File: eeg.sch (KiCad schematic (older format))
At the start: 145 parts, among them J1 USB_B_Mini, U1 STM32F446RE, U10 -.+2.5V.+3.3V-GND, U11 +5V, U12 RN4678-V_RM100, U13 ADS1299IPAG, U2 ADS1299-8CHANNEL, U3 LD39050PU33R, U4 TPS60403DBVT, U5 TPS73225DBVT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

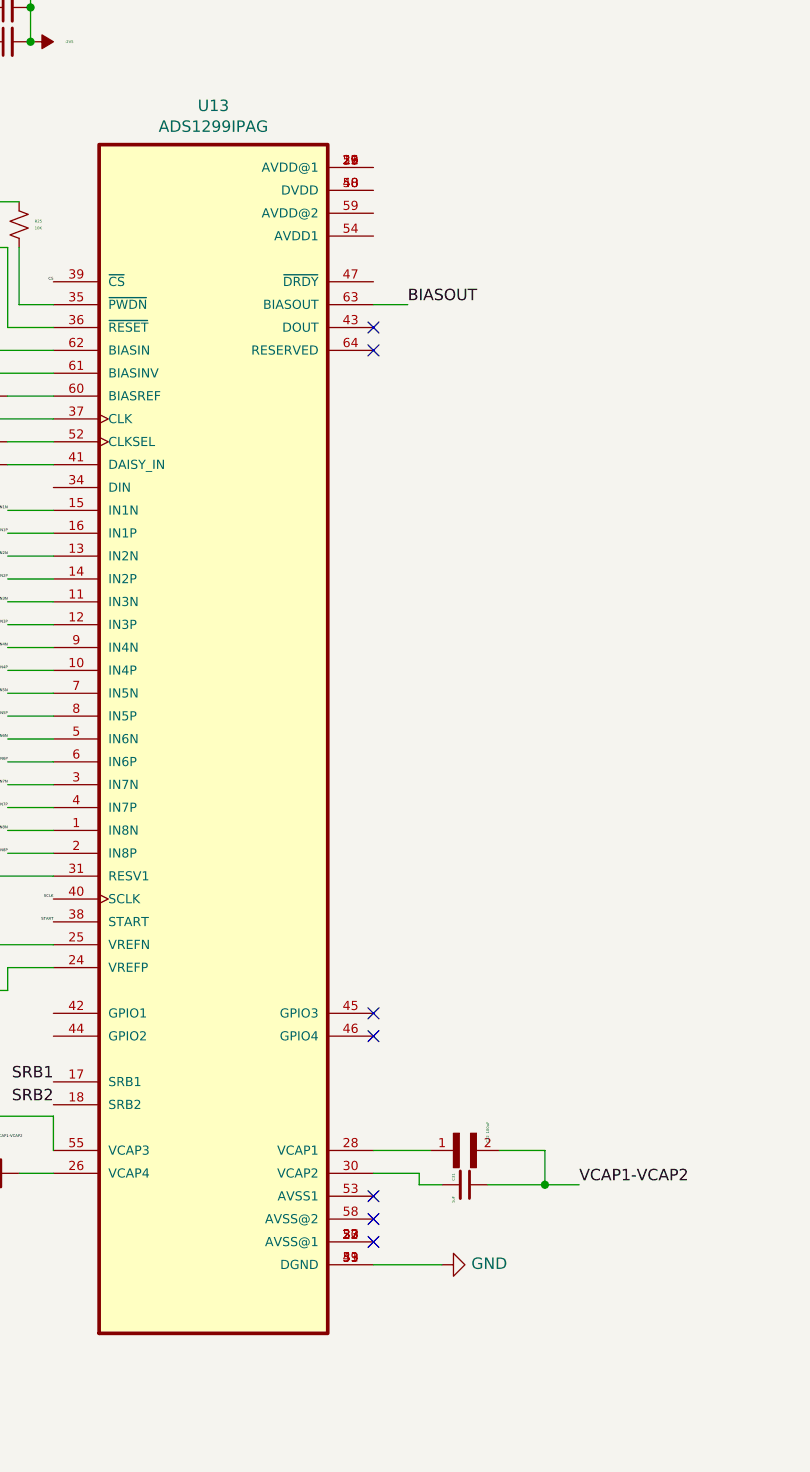
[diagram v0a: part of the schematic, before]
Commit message: ADS1299's SPI connections fixed and Supply pins should be checked
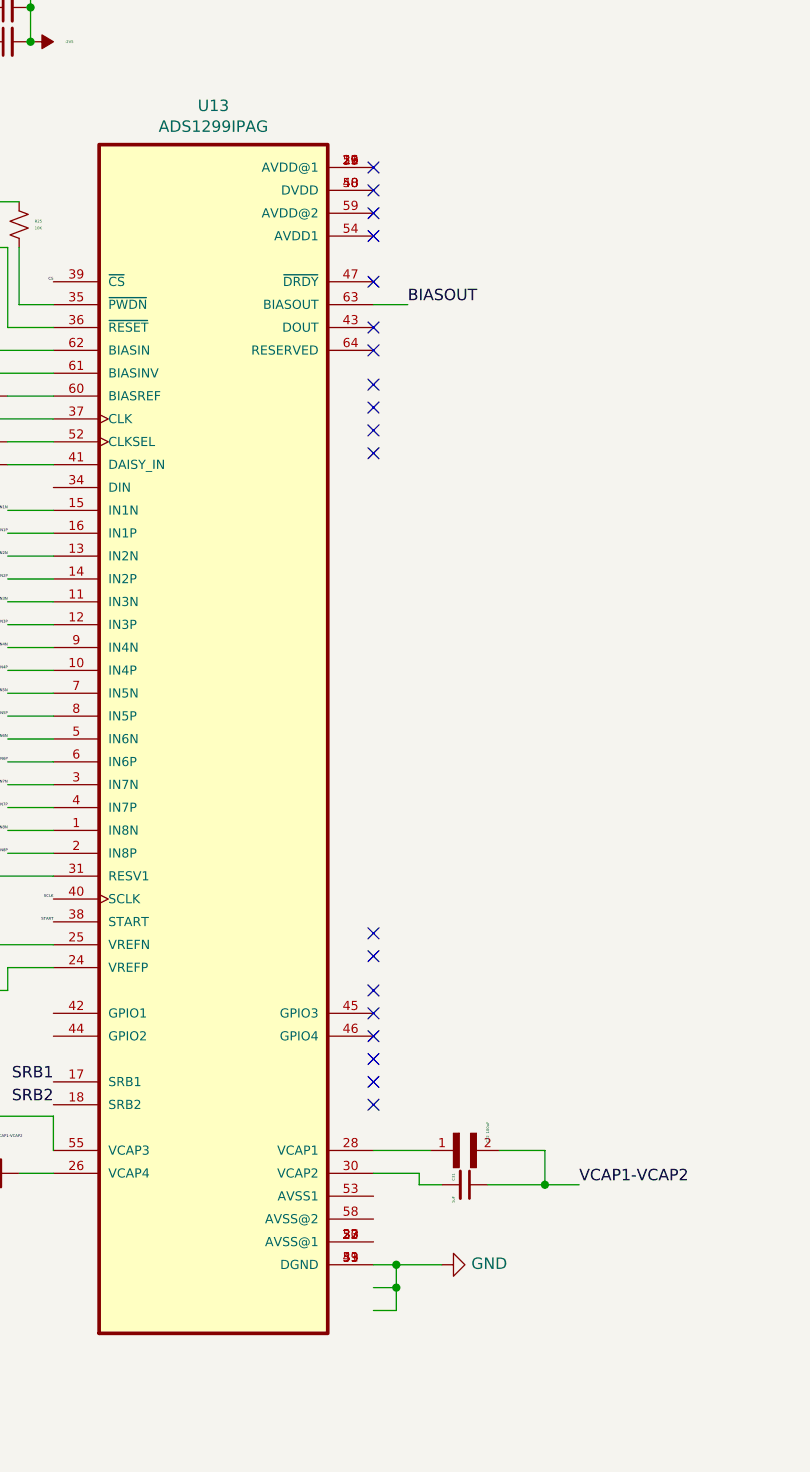
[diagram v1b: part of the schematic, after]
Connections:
- no-connect marks 82 -> 94
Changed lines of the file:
@@
-	1    0    0    -1
-$EndComp
-$Comp
-L ADS1299IPAG:ADS1299IPAG U13
-U 1 1 6000F5DE
-P 7350 13100
-F 0 "U13" H 7350 15870 50  0000 C CNN
-F 1 "ADS1299IPAG" H 7350 15779 50  0000 C CNN
-F 2 "QFP50P1200X1200X120-64N" H 7350 13100 50  0001 L BNN
-F 3 "" H 7350 13100 50  0001 L BNN
-	1    7350 13100
 	1    0    0    -1
 $EndComp
@@
 $EndComp
 Wire Wire Line
-	8050 15400 8350 15400
+	8050 15400 8150 15400
 Wire Wire Line
 	6300 15000 5950 15000
@@
 NoConn ~ 8050 14300
 NoConn ~ 8050 14400
-NoConn ~ 8050 15100
-NoConn ~ 8050 15200
-NoConn ~ 8050 15300
 NoConn ~ 8050 11300
 NoConn ~ 8050 11400
@@
 Wire Wire Line
 	12700 6650 12700 7150
+$Comp
+L ADS1299IPAG:ADS1299IPAG U13
+U 1 1 6000F5DE
+P 7350 13100
+F 0 "U13" H 7350 15870 50  0000 C CNN
+F 1 "ADS1299IPAG" H 7350 15779 50  0000 C CNN
+F 2 "QFP50P1200X1200X120-64N" H 7350 13100 50  0001 L BNN
+F 3 "" H 7350 13100 50  0001 L BNN
+	1    7350 13100
+	1    0    0    -1
+$EndComp
+Wire Wire Line
+	8050 15500 8150 15500
+Wire Wire Line
+	8150 15500 8150 15400
+Connection ~ 8150 15400
+Wire Wire Line
+	8150 15400 8350 15400
+Wire Wire Line
+	8050 15600 8150 15600
+Wire Wire Line
+	8150 15600 8150 15500
+Connection ~ 8150 15500
+NoConn ~ 8050 13950
+NoConn ~ 8050 14050
+NoConn ~ 8050 14200
+NoConn ~ 8050 14500
+NoConn ~ 8050 14600
+NoConn ~ 8050 14700
+NoConn ~ 8050 11550
+NoConn ~ 8050 11650
+NoConn ~ 8050 11750
+NoConn ~ 8050 11850
+NoConn ~ 8050 11100
+NoConn ~ 8050 10600
+NoConn ~ 8050 10700
+NoConn ~ 8050 10800
+NoConn ~ 8050 10900
 $EndSCHEMATC

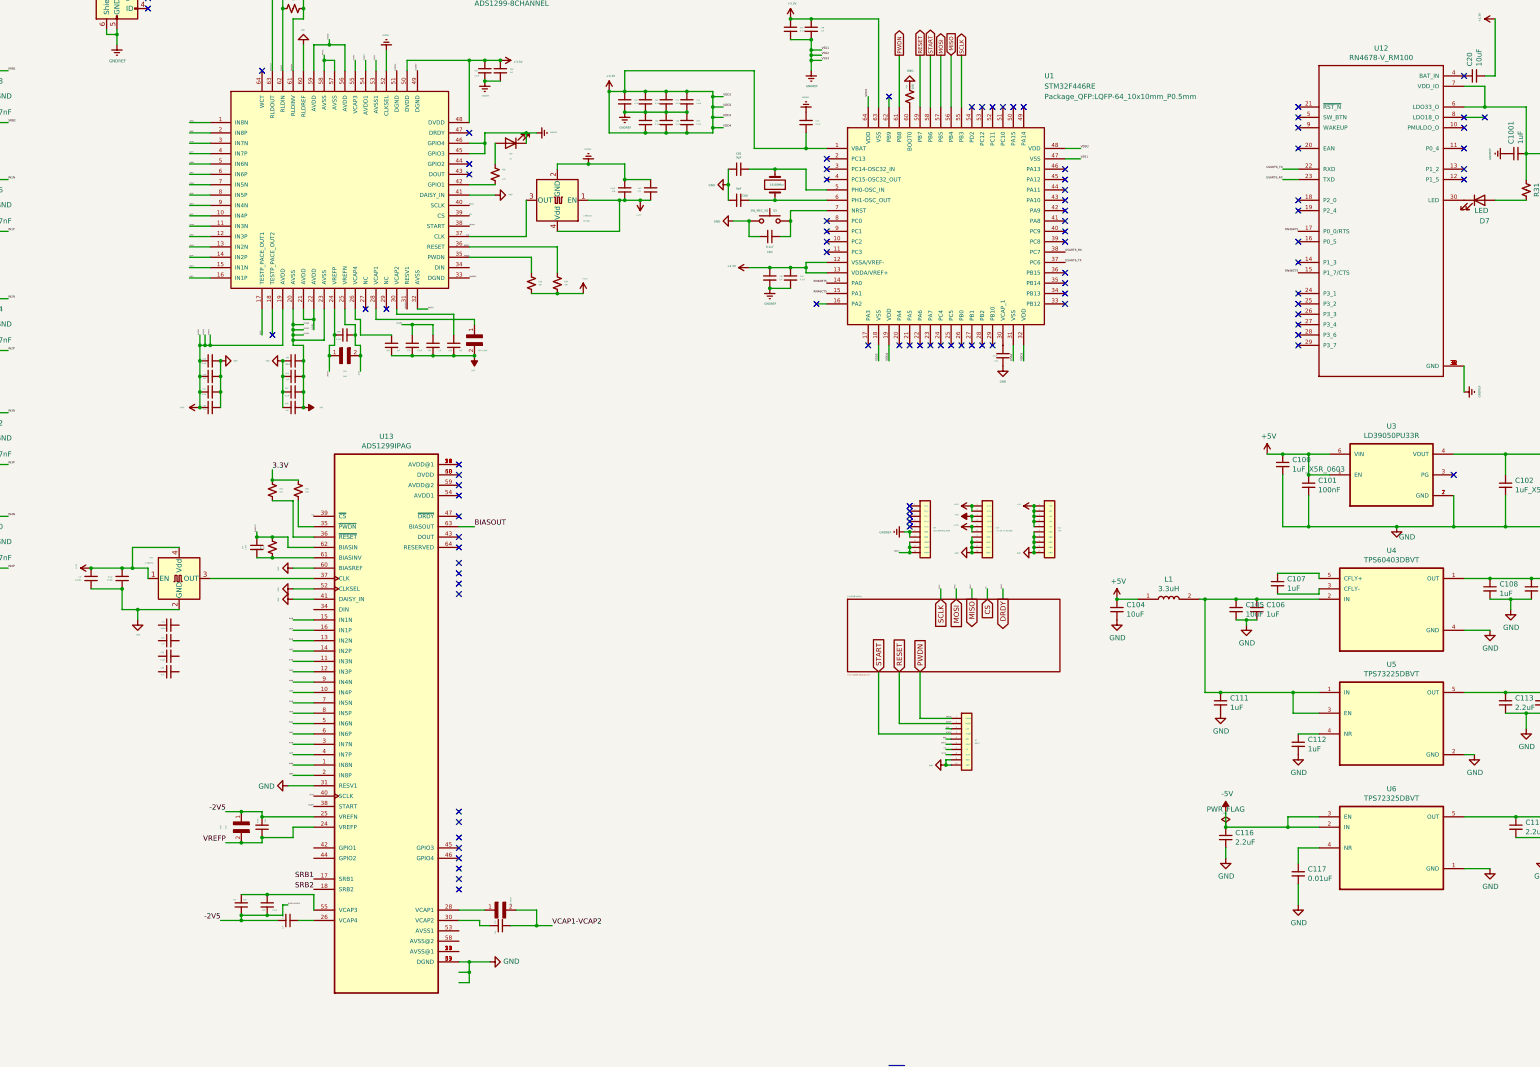
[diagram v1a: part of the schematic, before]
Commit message: ADS1299 Tracks fixed.
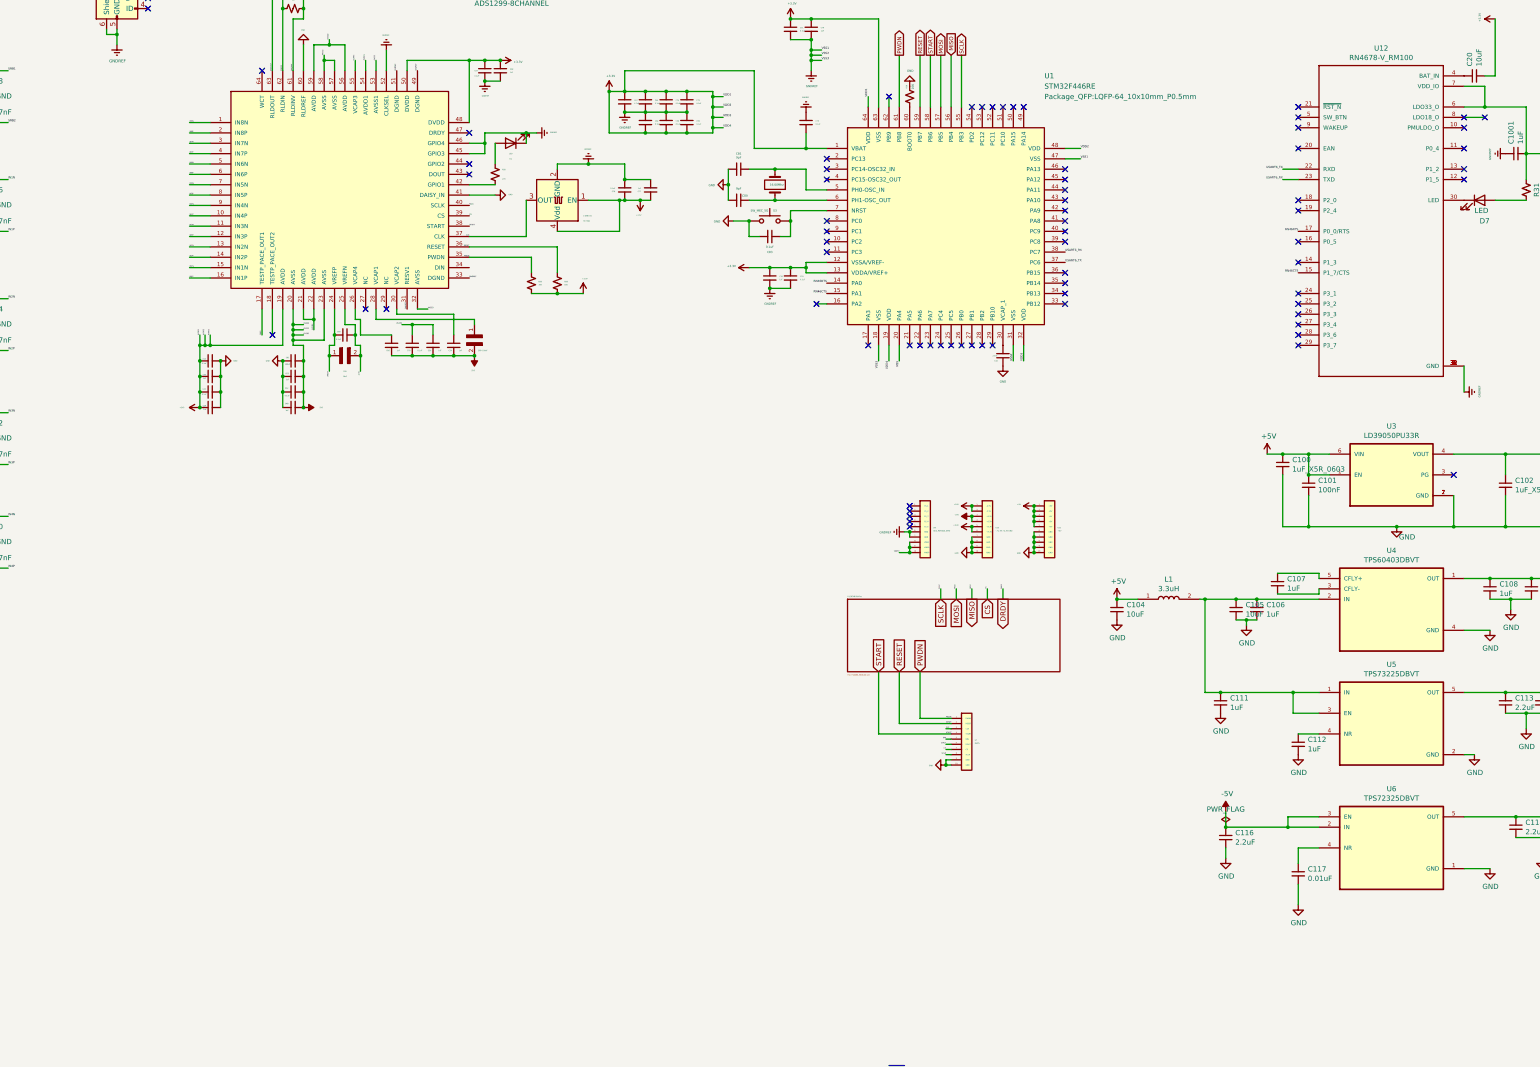
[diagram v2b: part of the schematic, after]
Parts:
- removed C1000, C23, C28, C29: 0.1uF, Capacitor_SMD:C_0603_1608Metric, symbol Device:C_Small
- removed C10001, C22, C24, C26, C30, C31: 1uF, Capacitor_SMD:C_0603_1608Metric, symbol Device:C_Small
- removed C21: 100uF, Capacitor_SMD:C_0603_1608Metric, symbol Device:C_Small
- removed C25: 10uF, TCA1C106M8R:RESC3216X65N, symbol TCA1C106M8R:TCA1C106M8R
- removed C27: 1.5nF, Capacitor_SMD:C_0805_2012Metric, symbol Device:C_Small
- removed C32: 100uF, TCA1C106M8R:RESC3216X65N, symbol TCA1C106M8R:TCA1C106M8R
- removed HC2: 2.048mhz, ERA-3A:OSCCC500X320X150N, symbol Oscillator:ASE-xxxMHz
- removed R23, R25: 10K, ERA-3A:RESC1608X55N, symbol Device:R_Small_US
- removed R24: 1M, ERA-6AEB105V:RESC2012X60N, symbol Device:R_Small_US
- removed U13: ADS1299IPAG, QFP50P1200X1200X120-64N, symbol ADS1299IPAG:ADS1299IPAG
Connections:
- net NSS: now reaches U1.20 (PA4)
- no-connect marks 94 -> 73

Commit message: Created hierarchical sheet
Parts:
- C65, C69: symbol TCA1C106M8R:TCA1C106M8R -> eeg-rescue:TCA1C106M8R-TCA1C106M8R
- L1, L2, L4, L5: symbol MLZ2012A3R3WT000:MLZ2012A3R3WT000 -> eeg-rescue:MLZ2012A3R3WT000-MLZ2012A3R3WT000
- U3: symbol LD39050PU33R:LD39050PU33R -> eeg-rescue:LD39050PU33R-LD39050PU33R
- U4: symbol TPS60403DBVT:TPS60403DBVT -> eeg-rescue:TPS60403DBVT-TPS60403DBVT
- U5: symbol TPS73225DBVT:TPS73225DBVT -> eeg-rescue:TPS73225DBVT-TPS73225DBVT
- U6: symbol TPS72325DBVT:TPS72325DBVT -> eeg-rescue:TPS72325DBVT-TPS72325DBVT
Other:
- moved on the sheet: C1, C10, C100, C1001, C101, C102, C103, C104, C105, C106, C107, C108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

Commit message: GND changed to GNDA
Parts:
- added D2, D3, D4: LED, LED_SMD:LED_0603_1608Metric, symbol Device:LED
- added J2: Conn_01x10_MountingPin, Connector_PinHeader_1.27mm:PinHeader_1x10_P1.27mm_Vertical, symbol Connector_Generic_MountingPin:Conn_01x10_MountingPin
- added R20, R21, R22: R_Small, symbol Device:R_Small
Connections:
- net labels added: GNDA, GNDD, SWCLK, SWDIO
- wire segments 429 -> 442
- no-connect marks 73 -> 71

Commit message: uC status leds added
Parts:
- removed U61: Electrode1, ADS1299IPAG:openldhardware, symbol eeg-rescue:Electrode-Electrode-eeg-rescue-eeg-rescue
- removed U8: Electrode2, ADS1299IPAG:openldhardware, symbol eeg-rescue:Electrode2-Electrode2
- added J3, J4: Conn_02x20_Counter_Clockwise, Connector_PinHeader_1.27mm:PinHeader_2x20_P1.27mm_Vertical, symbol Connector_Generic:Conn_02x20_Counter_Clockwise
- C1001: footprint (none) -> Capacitor_SMD:C_0603_1608Metric
- D1: footprint (none) -> LED_SMD:LED_0603_1608Metric
- R20, R21, R22: footprint (none) -> Resistor_SMD:R_0603_1608Metric
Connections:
- no-connect marks 71 -> 68

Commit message: SPI3 changed to SPI1
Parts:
- removed J2: Conn_01x10_MountingPin, Connector_PinHeader_1.27mm:PinHeader_1x10_P1.27mm_Vertical, symbol Connector_Generic_MountingPin:Conn_01x10_MountingPin
- removed S3: SW_MEC_5G, Button_Switch_SMD:SW_SPST_B3U-1000P, symbol Switch:SW_MEC_5G
- added J2: Conn_01x10, Connector_PinHeader_1.27mm:PinHeader_1x10_P1.27mm_Vertical, symbol Connector_Generic:Conn_01x10
- added SW3: EVQ-Q2K03W, EVQ-Q2K03W_PAN, symbol 2021-02-28_21-16-32:EVQ-Q2K03W
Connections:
- net labels added: SCK
- net labels removed: GND, NSS
- wire segments 442 -> 445
- no-connect marks 68 -> 65
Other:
- moved on the sheet: C74, C76, C83, D2, D3, D4

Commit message: Connectors change 1.27mm to 2.54mm and 20 pins to 10 pins
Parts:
- removed C1001: 1uF, Capacitor_SMD:C_0603_1608Metric, symbol Device:C_Small
- removed J2: Conn_01x10, Connector_PinHeader_1.27mm:PinHeader_1x10_P1.27mm_Vertical, symbol Connector_Generic:Conn_01x10
- removed J3, J4: Conn_02x20_Counter_Clockwise, Connector_PinHeader_1.27mm:PinHeader_2x20_P1.27mm_Vertical, symbol Connector_Generic:Conn_02x20_Counter_Clockwise
- removed U10: -.+2.5V.+3.3V-GND, Connector_PinSocket_1.27mm:PinSocket_1x10_P1.27mm_Vertical, symbol eeg-rescue:-.+2.5V.+3.3V-GND-Data10Pin
- removed U11: +5V, Connector_PinSocket_1.27mm:PinSocket_1x10_P1.27mm_Vertical, symbol eeg-rescue:+5V-Data10Pin
- removed U7: DATA, Connector_PinSocket_1.27mm:PinSocket_1x10_P1.27mm_Vertical, symbol eeg-rescue:DATA-Data10Pin-eeg-rescue
- removed U9: ADC_REFGND_GPIO, Connector_PinSocket_1.27mm:PinSocket_1x10_P1.27mm_Vertical, symbol eeg-rescue:ADC_REFGND_GPIO-Data10Pin
- added J1, J2, J3, J4: Conn_01x05_Male, Connector_PinHeader_2.54mm:PinHeader_1x05_P2.54mm_Vertical, symbol Connector:Conn_01x05_Male
- added J5: Conn_01x10, Connector_PinHeader_1.27mm:PinHeader_1x10_P1.27mm_Vertical, symbol Connector_Generic:Conn_01x10
- added J6, J7: Conn_01x10_Male, Connector_PinSocket_2.54mm:PinSocket_1x10_P2.54mm_Vertical, symbol Connector:Conn_01x10_Male
- SW3: footprint EVQ-Q2K03W_PAN -> footprints:EVQ-Q2K03W
- renumbered J1 to J10
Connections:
- net labels removed: +2.5V, -2.5V, GNDREF, LD033_O, SCK
- wire segments 445 -> 430
- no-connect marks 65 -> 60
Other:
- moved on the sheet: C20, C77, C78, D1, D2, D3, D4, HC7361, R32

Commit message: ground tracks removed
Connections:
- wire segments 430 -> 428
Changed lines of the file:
@@
 Wire Wire Line
 	7250 10850 7250 10700
-Wire Wire Line
-	7250 10700 7350 10700
 $Comp
 L power:GNDA #PWR0169
@@
 	0    1    1    0
 $EndComp
-Connection ~ 7250 10700
 Text Label 7450 10850 1    50   ~ 0
 SCLK
@@
 Text Label 8150 10850 1    50   ~ 0
 PWDN
-Wire Wire Line
-	7350 10850 7350 10700
 Text Label 7550 10850 1    50   ~ 0
 CS
@@
 Wire Wire Line
 	8150 1500 8600 1500
+Text GLabel 8350 1400 2    50   Input ~ 0
+SWCLK
 Text GLabel 8650 1300 2    50   Input ~ 0
-SWCLK
-Text GLabel 8350 1400 2    50   Input ~ 0
 SWDIO
 Wire Wire Line
 	8150 1300 8650 1300
+Text Label 7350 10850 1    50   ~ 0
+DRDY
 $EndSCHEMATC
